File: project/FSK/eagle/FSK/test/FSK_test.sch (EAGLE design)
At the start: 20 parts, among them X1 SMA-142-0711-821/826, X2 SMA-142-0711-821/826, X3 SMA-142-0711-821/826, X4 SMA-142-0711-821/826, X5 SMA-142-0711-821/826

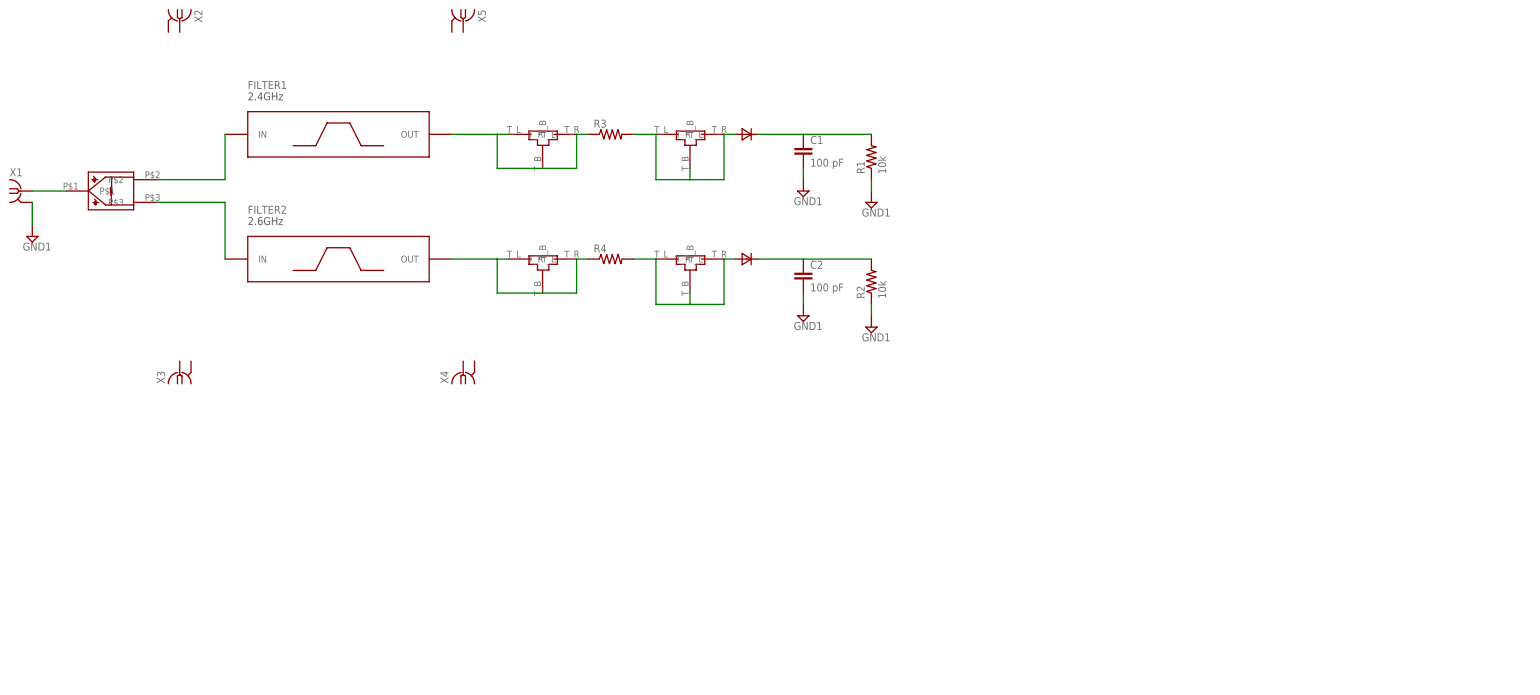
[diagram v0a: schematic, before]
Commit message: fixed footprints for comp. and  SSD driver
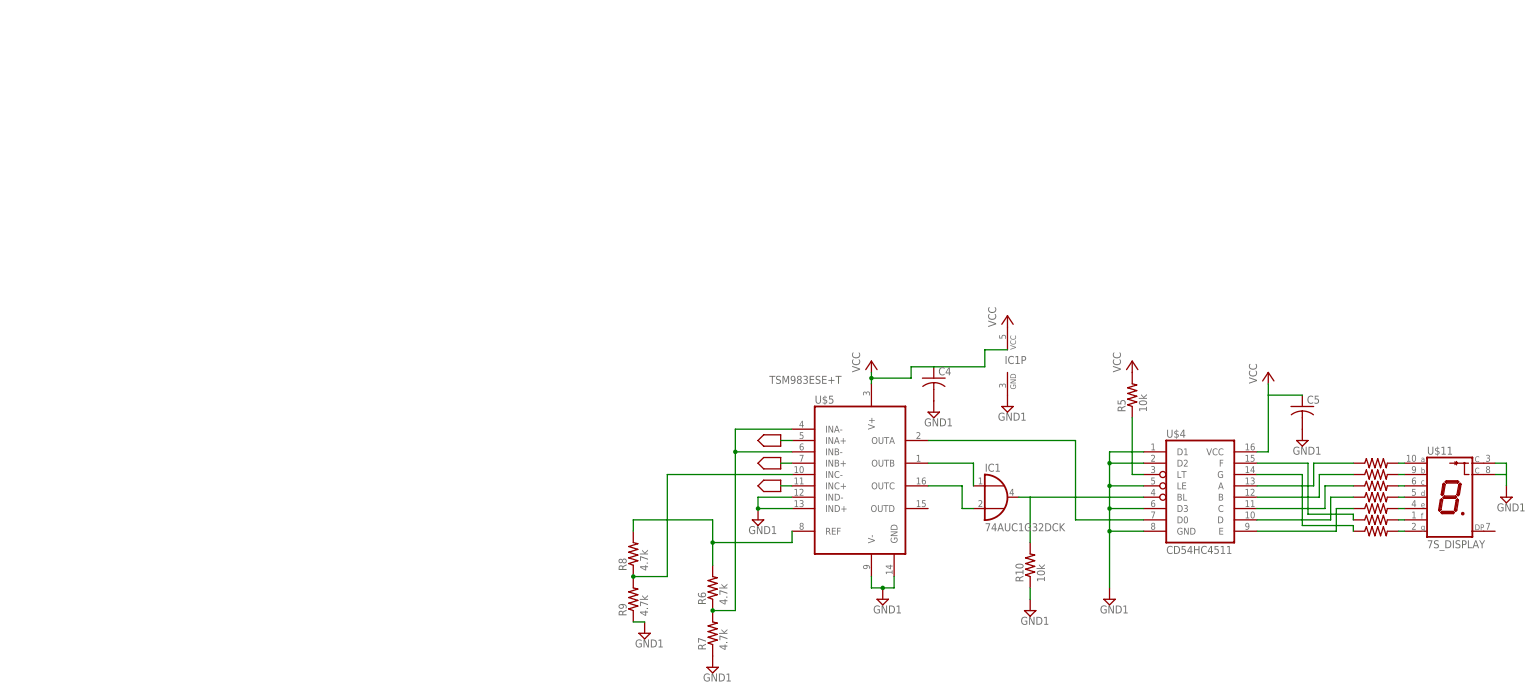
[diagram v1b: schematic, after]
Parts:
- removed 2.4FIL, 2.4TUNED, 2.6FIL, 2.6TUNED: TEE_TL1, ECE532_Parts:TEE_TL1
- removed C1, C2: 100 pF, rcl:C-EUC0603
- removed FILTER1: 2.4GHz, ECE532_Parts:1IN_PIPE_CAP
- removed FILTER2: 2.6GHz, ECE532_Parts:1IN_PIPE_CAP
- removed R1, R2: 10k, rcl:R-US_M1206
- removed R3, R4: (no value), rcl:R-US_R0603
- removed U$1: WSPLITTER_2.5GHZ, ECE532_Parts:WSPLITTER_2.5GHZ
- removed U$2, U$3: HSMS-2850, ECE532_Parts:HSMS-2850
- removed X1, X2, X3, X4, X5: SMA-142-0711-821/826, con-coax:SMA-142-0711-821/826
- added C4, C5: (no value), rcl:C-USC0603
- added IC1: 74AUC1G32DCK, 74xx-little-de:74AUC1G32DCK
- added R10, R5: 10k, rcl:R-US_R1206
- added R11, R12, R13, R14, R15, R16, R17: (no value), rcl:R-US_R0603
- added R6, R7, R8, R9: 4.7k, rcl:R-US_R1206
- added U$11: 7S_DISPLAY, ECE532_Parts:7S_DISPLAY
- added U$4: CD54HC4511, ECE532_Parts:CD54HC4511
- added U$5: TSM983ESE+T, ECE532_Parts:TSM983ESE+T
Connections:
- removed net 2.4FIL: 2.4FIL.T_B, 2.4FIL.T_L, 2.4FIL.T_R, FILTER1.OUT, R3.1
- removed net 2.4GHZ: FILTER1.IN, U$1.P$2
- removed net 2.4TUNED: 2.4TUNED.T_B, 2.4TUNED.T_L, 2.4TUNED.T_R, R3.2, U$2.A
- removed net 2.6FIL: 2.6FIL.T_B, 2.6FIL.T_L, 2.6FIL.T_R, FILTER2.OUT, R4.1
- removed net 2.6GHZ: FILTER2.IN, U$1.P$3
- removed net 2.6TUNED: 2.6TUNED.T_B, 2.6TUNED.T_L, 2.6TUNED.T_R, R4.2, U$3.A
- removed net N$5: U$1.P$1, X1.1
- new net 2.4_OUT: U$5.INA+
- new net 2.6_OUT: U$5.INB+, U$5.INC+
- new net N$1: IC1A.O, R10.2, U$4.BL
- new net N$10: R6.2, R8.2, U$5.REF
- new net N$11: R6.1, R7.2, U$5.INA-, U$5.INB-
- new net N$12: R5.1, U$4.LT
- new net N$13: R14.2, U$11.D
- new net N$14: R15.2, U$11.E
- new net N$15: R16.2, U$11.F
- new net N$16: R17.2, U$11.G
- new net N$17: R11.1, U$4.A
- new net N$18: R12.1, U$4.B
- new net N$19: R13.1, U$4.C
- new net N$2: IC1A.I0, U$5.OUTB
- new net N$20: R14.1, U$4.D
- new net N$21: R15.1, U$4.E
- new net N$22: R16.1, U$4.F
- new net N$23: R17.1, U$4.G
- new net N$6: U$4.D0, U$5.OUTA
- new net N$7: R13.2, U$11.C
- new net N$8: IC1A.I1, U$5.OUTC
- new net N$9: R8.1, R9.2, U$5.INC-
- new net VCC: C4.1, C5.1, IC1P.VCC, R5.2, U$4.VCC, U$5.V+
- net GND1: now also C4.2, C5.2, IC1P.GND, R10.1, R7.1, R9.1, U$11.C@1, U$11.C@2, U$4.D1, U$4.D2, U$4.D3, U$4.GND, U$4.LE, U$5.GND, U$5.IND+, U$5.IND-, U$5.V-; no longer C1.2, C2.2, R1.1, R2.1, X1.2
- net N$3: now also R11.2, U$11.A; no longer C1.1, R1.2, U$2.C
- net N$4: now also R12.2, U$11.B; no longer C2.1, R2.2, U$3.C
